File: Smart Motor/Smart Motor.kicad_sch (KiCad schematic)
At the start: 31 parts, among them J1 Conn_01x04_Socket, U1 TMC2209-LA, U2 TPS54360DDA, U3 AMS1117-3.3, U4 AS5600L-ASOM

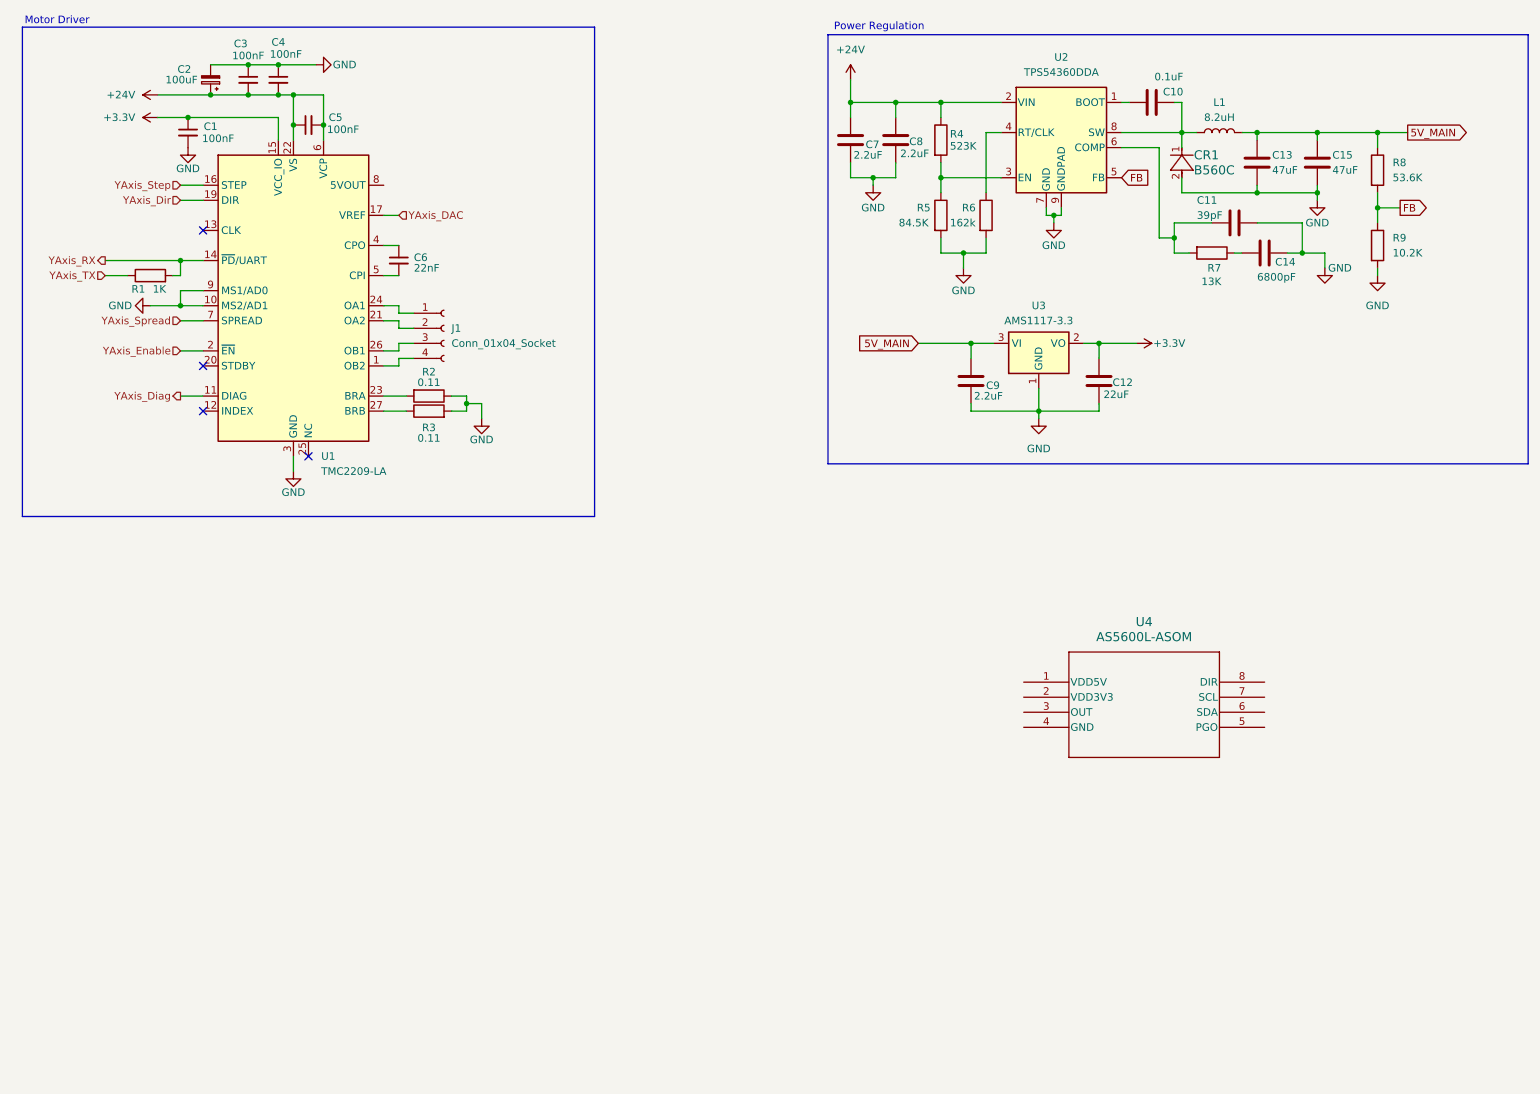
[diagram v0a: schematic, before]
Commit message: Finished initial design of motor PCB
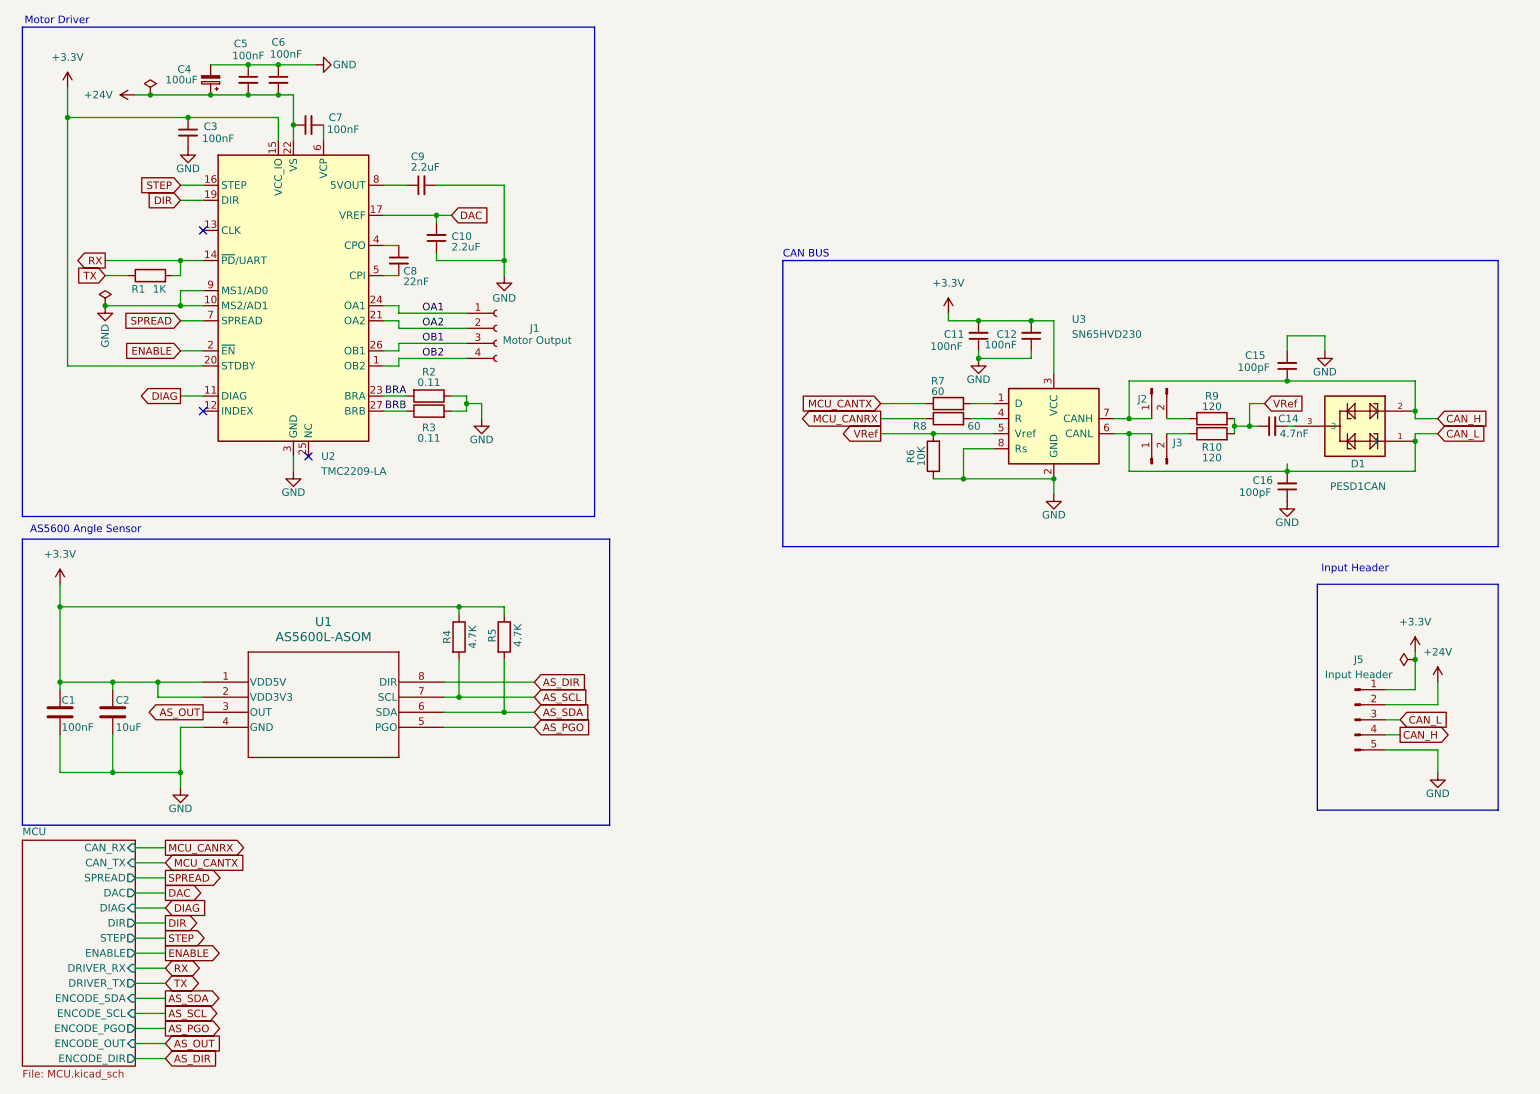
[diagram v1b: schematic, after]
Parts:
- removed C10: 0.1uF, Capacitor_SMD:C_0603_1608Metric_Pad1.08x0.95mm_HandSolder, symbol Device:C
- removed C11: 39pF, Capacitor_SMD:C_0603_1608Metric_Pad1.08x0.95mm_HandSolder, symbol Device:C
- removed C12: 22uF, Capacitor_SMD:C_0603_1608Metric_Pad1.08x0.95mm_HandSolder, symbol Device:C
- removed C13, C15: 47uF, Capacitor_SMD:C_0603_1608Metric_Pad1.08x0.95mm_HandSolder, symbol Device:C
- removed C14: 6800pF, Capacitor_SMD:C_0603_1608Metric_Pad1.08x0.95mm_HandSolder, symbol Device:C
- removed C7, C8, C9: 2.2uF, Capacitor_SMD:C_0603_1608Metric_Pad1.08x0.95mm_HandSolder, symbol Device:C
- removed CR1: B560C, B560C-13-F-Schottky Diode:SMC_DIO, symbol B560C-13-F:B560C-13-F
- removed L1: 8.2uH, Inductor_SMD:L_0603_1608Metric_Pad1.05x0.95mm_HandSolder, symbol Device:L
- removed U2: TPS54360DDA, Package_SO:TI_SO-PowerPAD-8_ThermalVias, symbol Regulator_Switching:TPS54360DDA
- removed U3: AMS1117-3.3, Package_TO_SOT_SMD:SOT-223-3_TabPin2, symbol Regulator_Linear:AMS1117-3.3
- added C1: 100nF, Capacitor_SMD:C_0603_1608Metric_Pad1.08x0.95mm_HandSolder, symbol Device:C
- added C10, C9: 2.2uF, Capacitor_SMD:C_0603_1608Metric_Pad1.08x0.95mm_HandSolder, symbol Device:C_Small
- added C11, C12: 100nF, Capacitor_SMD:C_0603_1608Metric_Pad1.08x0.95mm_HandSolder, symbol Device:C_Small
- added C14: 4.7nF, Capacitor_SMD:C_0603_1608Metric_Pad1.08x0.95mm_HandSolder, symbol Device:C_Small
- added C15, C16: 100pF, Capacitor_SMD:C_0603_1608Metric_Pad1.08x0.95mm_HandSolder, symbol Device:C_Small
- added C2: 10uF, Capacitor_SMD:C_0603_1608Metric_Pad1.08x0.95mm_HandSolder, symbol Device:C
- added D1: PESD1CAN, PESD1CAN:SOT23-3, symbol PESD1CAN:PESD1CAN
- added J2, J3: Conn_01x02_Pin, Connector_PinHeader_2.54mm:PinHeader_1x02_P2.54mm_Vertical, symbol Connector:Conn_01x02_Pin
- added J5: Input Header, Connector_JST:JST_XH_B5B-XH-A_1x05_P2.50mm_Vertical, symbol Connector:Conn_01x05_Pin
- added R10: 120, Resistor_SMD:R_0603_1608Metric_Pad0.98x0.95mm_HandSolder, symbol Device:R
- added U3: SN65HVD230, Package_SO:SOIC-8_3.9x4.9mm_P1.27mm, symbol Interface_CAN_LIN:SN65HVD230
- C4: renamed from C2; footprint Capacitor_Tantalum_SMD:CP_EIA-1608-10_AVX-L_HandSolder -> Capacitor_SMD:C_1210_3225Metric
- C5: renamed from C3; footprint Capacitor_SMD:C_0603_1608Metric_Pad1.08x0.95mm_HandSolder -> Capacitor_SMD:C_1210_3225Metric
- C6: renamed from C4; footprint Capacitor_SMD:C_0603_1608Metric_Pad1.08x0.95mm_HandSolder -> Capacitor_SMD:C_1210_3225Metric
- C7: renamed from C5; footprint Capacitor_SMD:C_0603_1608Metric_Pad1.08x0.95mm_HandSolder -> Capacitor_SMD:C_1210_3225Metric
- J1: value Conn_01x04_Socket -> Motor Output
- R4: value 523K -> 4.7K
- R5: value 84.5K -> 4.7K
- R6: value 162k -> 10K
- R7: value 13K -> 60
- R8: value 53.6K -> 60
- R9: value 10.2K -> 120
- U1: renamed from U4; footprint AS5600L-ASOM_AMS -> AS5600L:AS5600L-ASOM_AMS-M
- renumbered C1 to C3, C6 to C8, U1 to U2
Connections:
- net +24V: now also J5.2 (Pin_2); no longer C7.2, R4.1, U2.6 (VCP)
- net +3.3V: now also R4.1, R5.1, U1.1 (VDD5V), U1.2 (VDD3V3), U2.20 (STDBY), C1.2, C11.2, C12.2, C2.2, J5.1 (Pin_1), U3.3 (VCC)
- net GND: now also R6.1, U1.4 (GND), C1.1, C10.1, C11.1, C12.1, C15.2, C16.1, C2.1, C9.2, J5.5 (Pin_5), U3.2 (GND), U3.8 (Rs); no longer R5.2, R6.2, R9.2
- net AS_OUT: now reaches U1.3 (OUT)
- net AS_PGO: now reaches U1.5 (PGO)
- net AS_SDA: now reaches U1.6 (SDA)
- net AS_SDA: now also R5.2
- net AS_SCL: now reaches U1.7 (SCL)
- net AS_SCL: now also R4.2
- net AS_DIR: now reaches U1.8 (DIR)
- net BRB: now reaches R3.1, U2.27 (BRB)
- net BRA: now reaches R2.2, U2.23 (BRA)
- net at R7.2: now also U3.1 (D)
- net MCU_CANTX: now reaches R7.1
- net OB2: now reaches J1.4 (Pin_4), U2.1 (OB2)
- net OA2: now reaches J1.2 (Pin_2), U2.21 (OA2)
- net OA1: now reaches J1.1 (Pin_1), U2.24 (OA1)
- net OB1: now reaches J1.3 (Pin_3), U2.26 (OB1)
- net at U2.8 (5VOUT): now also C9.1
- net 5V_MAIN renamed MCU_CANRX
- net FB: no longer names the net of R9.1
- net FB: now also J2.2 (Pin_2); no longer R8.2
- net YAxis_DAC renamed DAC
- net DAC: now also C10.2
- net YAxis_Diag renamed DIAG
- net YAxis_Dir renamed DIR
- net YAxis_Enable renamed ENABLE
- net YAxis_RX renamed RX
- net YAxis_Spread renamed SPREAD
- net YAxis_Step renamed STEP
- net YAxis_TX renamed TX
- new net: J3.2 (Pin_2), R10.1
- new net: R8.2, U3.4 (R)
- new net: C14.2, D1.3
- new net: C7.2, U2.6 (VCP)
- new net CAN_H: C15.1, D1.2, J2.1 (Pin_1), J5.4 (Pin_4), U3.7 (CANH)
- new net CAN_L: C16.2, D1.1, J3.1 (Pin_1), J5.3 (Pin_3), U3.6 (CANL)
- new net VRef: C14.1, R10.2, R6.2, R9.2, U3.5 (Vref)
- no-connect marks 4 -> 3
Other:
- added sheet MCU (MCU.kicad_sch)
- note added: "AS5600 Angle Sensor"
- note added: "CAN BUS"
- note added: "Input Header"
- note removed: "Power Regulation"
- moved on the sheet: J1, U1
